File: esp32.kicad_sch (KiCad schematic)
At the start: 4 parts, among them U1 ESP32-S3-WROOM-1

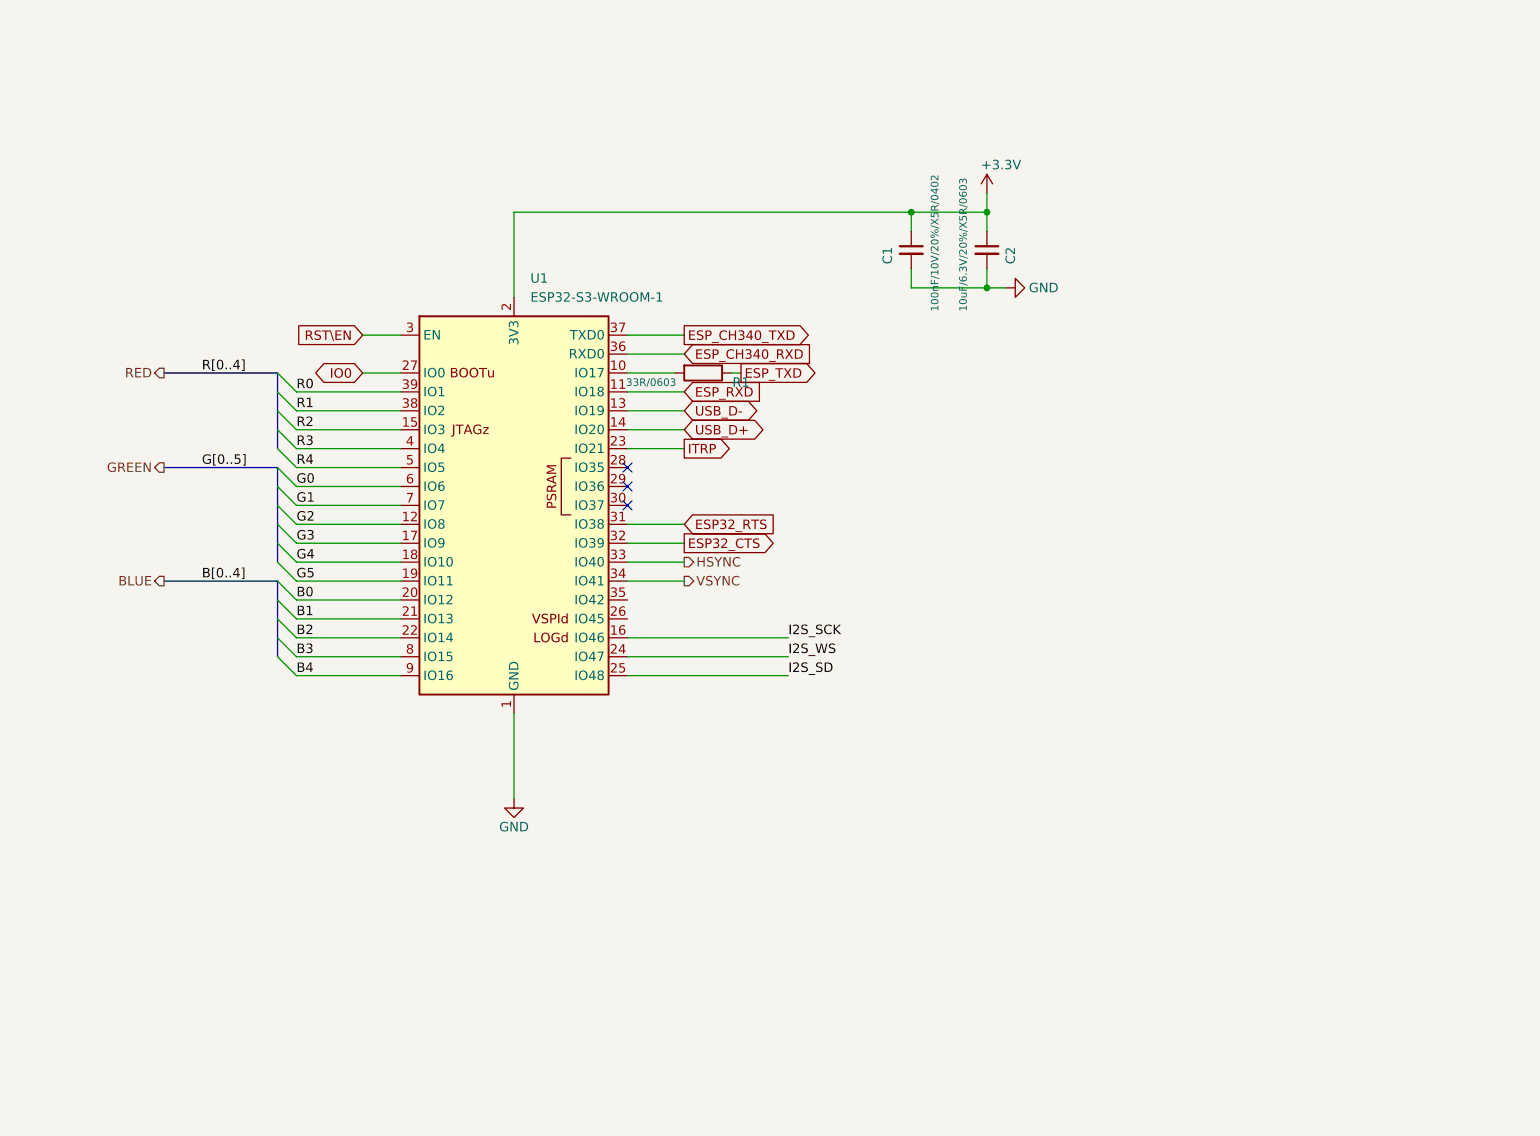
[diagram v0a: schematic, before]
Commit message: schematics finished, pcb routing 80%
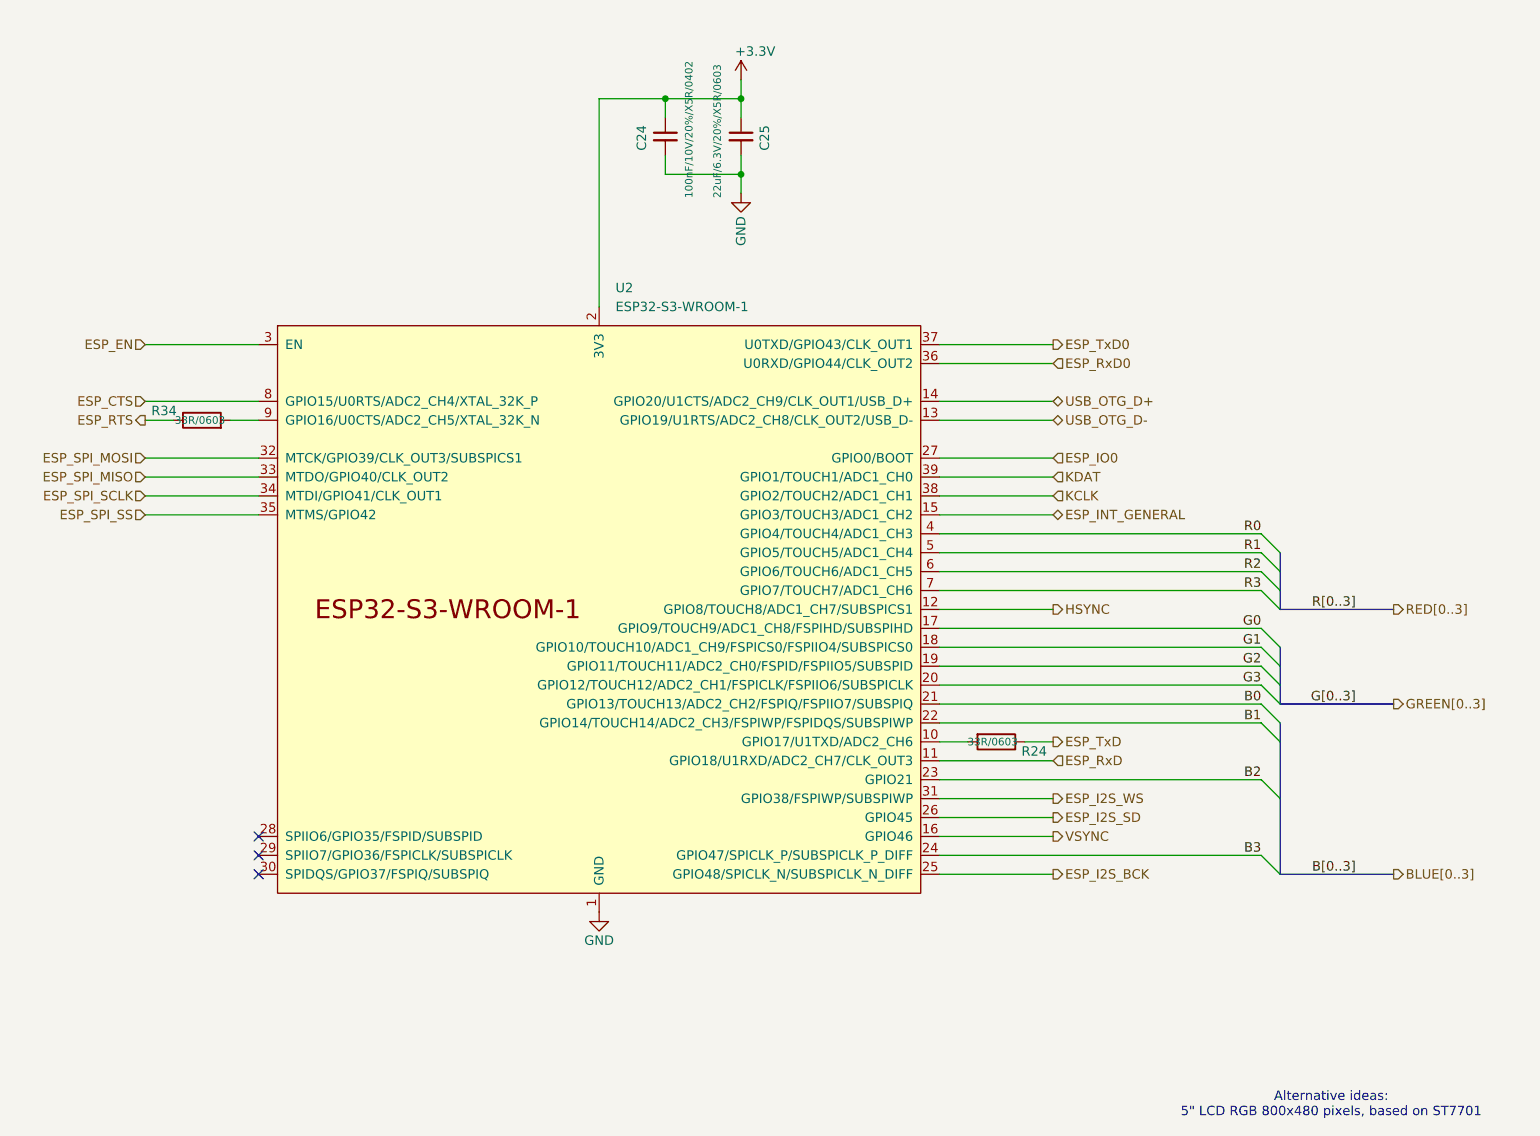
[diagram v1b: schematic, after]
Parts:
- removed C1: 100nF/10V/20%/X5R/0402, OLIMEX_RLC-FP:C_0402_5MIL_DWS, symbol AgonLight2_Rev_B:C
- removed C2: 10uF/6.3V/20%/X5R/0603, OLIMEX_RLC-FP:C_0603_5MIL_DWS, symbol AgonLight2_Rev_B:C
- removed R1: 33R/0603, OLIMEX_RLC-FP:R_0603_5MIL_DWS, symbol AgonLight2_Rev_B:R
- removed U1: ESP32-S3-WROOM-1, RF_Module:ESP32-S3-WROOM-1, symbol RF_Module:ESP32-S3-WROOM-1
- added C24: 100nF/10V/20%/X5R/0402, HexAgonFootprintsLibrary:C_0402_5MIL_DWS, symbol AgonLight2_Rev_B:C
- added C25: 22uF/6.3V/20%/X5R/0603, HexAgonFootprintsLibrary:C_0603_5MIL_DWS, symbol AgonLight2_Rev_B:C
- added R24, R34: 33R/0603, HexAgonFootprintsLibrary:R_0603_5MIL_DWS, symbol AgonLight2_Rev_B:R
- added U2: ESP32-S3-WROOM-1, Espressif:ESP32-S3-WROOM-1, symbol espressif:ESP32-S3-WROOM-1
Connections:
- net +3.3V: now also C24.1, C25.1, U2.2 (3V3)
- net B0: now also U2.21 (GPIO13/TOUCH13/ADC2_CH2/FSPIQ/FSPIIO7/SUBSPIQ)
- net B1: now also U2.22 (GPIO14/TOUCH14/ADC2_CH3/FSPIWP/FSPIDQS/SUBSPIWP)
- net B2: now also U2.23 (GPIO21)
- net B3: now also U2.24 (GPIO47/SPICLK_P/SUBSPICLK_P_DIFF)
- net G0: now also U2.17 (GPIO9/TOUCH9/ADC1_CH8/FSPIHD/SUBSPIHD)
- net G1: now also U2.18 (GPIO10/TOUCH10/ADC1_CH9/FSPICS0/FSPIIO4/SUBSPICS0)
- net G2: now also U2.19 (GPIO11/TOUCH11/ADC2_CH0/FSPID/FSPIIO5/SUBSPID)
- net G3: now also U2.20 (GPIO12/TOUCH12/ADC2_CH1/FSPICLK/FSPIIO6/SUBSPICLK)
- net GND: now also C24.2, C25.2, U2.1 (GND), U2.40 (GND), U2.41 (GND)
- net HSYNC: now also U2.12 (GPIO8/TOUCH8/ADC1_CH7/SUBSPICS1)
- net R0: now also U2.4 (GPIO4/TOUCH4/ADC1_CH3)
- net R1: now also U2.5 (GPIO5/TOUCH5/ADC1_CH4)
- net R2: now also U2.6 (GPIO6/TOUCH6/ADC1_CH5)
- net R3: now also U2.7 (GPIO7/TOUCH7/ADC1_CH6)
- net VSYNC: now also U2.16 (GPIO46)
- new net: R34.2, U2.9 (GPIO16/U0CTS/ADC2_CH5/XTAL_32K_N)
- new net: R24.2, U2.10 (GPIO17/U1TXD/ADC2_CH6)
- new net ESP_CTS: U2.8 (GPIO15/U0RTS/ADC2_CH4/XTAL_32K_P)
- new net ESP_EN: U2.3 (EN)
- new net ESP_I2S_BCK: U2.25 (GPIO48/SPICLK_N/SUBSPICLK_N_DIFF)
- new net ESP_I2S_SD: U2.26 (GPIO45)
- new net ESP_I2S_WS: U2.31 (GPIO38/FSPIWP/SUBSPIWP)
- new net ESP_INT_GENERAL: U2.15 (GPIO3/TOUCH3/ADC1_CH2)
- new net ESP_IO0: U2.27 (GPIO0/BOOT)
- new net ESP_RTS: R34.1
- new net ESP_RxD: U2.11 (GPIO18/U1RXD/ADC2_CH7/CLK_OUT3)
- new net ESP_RxD0: U2.36 (U0RXD/GPIO44/CLK_OUT2)
- new net ESP_SPI_MISO: U2.33 (MTDO/GPIO40/CLK_OUT2)
- new net ESP_SPI_MOSI: U2.32 (MTCK/GPIO39/CLK_OUT3/SUBSPICS1)
- new net ESP_SPI_SCLK: U2.34 (MTDI/GPIO41/CLK_OUT1)
- new net ESP_SPI_SS: U2.35 (MTMS/GPIO42)
- new net ESP_TxD: R24.1
- new net ESP_TxD0: U2.37 (U0TXD/GPIO43/CLK_OUT1)
- new net KCLK: U2.38 (GPIO2/TOUCH2/ADC1_CH1)
- new net KDAT: U2.39 (GPIO1/TOUCH1/ADC1_CH0)
- new net USB_OTG_D+: U2.14 (GPIO20/U1CTS/ADC2_CH9/CLK_OUT1/USB_D+)
- new net USB_OTG_D-: U2.13 (GPIO19/U1RTS/ADC2_CH8/CLK_OUT2/USB_D-)
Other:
- note added: "Alternative ideas: 5" LCD RGB 800x480 pixels, based on ST7701"

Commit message: 1st production and BOM
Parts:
- C24: MfgNumber (none) -> GRM022R61A104KE01L
- C25: value 22uF/6.3V/20%/X5R/0603 -> 22uF/6.3V/20%/X5R/C0603; MfgNumber (none) -> GRM188R60J226MEA0D
- R24, R34: MfgNumber (none) -> ESR03EZPJ330
- U2: MfgNumber (none) -> ESP32-S3-WROOM-1-N16R8
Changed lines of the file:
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@@
 			)
 		)
-		(property "Value" "22uF/6.3V/20%/X5R/0603"
+		(property "Value" "22uF/6.3V/20%/X5R/C0603"
 			(at 150.495 52.705 90)
 			(effects
@@
 				)
 				(hide yes)
+			)
+		)
+		(property "Note" ""
+			(at 153.67 44.45 0)
+			(effects
+				(font
+					(size 1.27 1.27)
+				)
+			)
+		)
+		(property "MfgNumber" "GRM188R60J226MEA0D"
+			(at 153.67 44.45 0)
+			(effects
+				(font
+					(size 1.27 1.27)
+				)
 			)
 		)
@@
 			)
 		)
+		(property "Note" ""
+			(at 143.51 44.45 0)
+			(effects
+				(font
+					(size 1.27 1.27)
+				)
+			)
+		)
+		(property "MfgNumber" "GRM022R61A104KE01L"
+			(at 143.51 44.45 0)
+			(effects
+				(font
+					(size 1.27 1.27)
+				)
+			)
+		)
 		(pin "1"
 		)
@@
 				)
 				(hide yes)
+			)
+		)
+		(property "Note" ""
+			(at 81.28 82.55 0)
+			(effects
+				(font
+					(size 1.27 1.27)
+				)
+			)
+		)
+		(property "MfgNumber" "ESR03EZPJ330"
+			(at 81.28 82.55 0)
+			(effects
+				(font
+					(size 1.27 1.27)
+				)
 			)
 		)
@@
 			)
 		)
+		(property "Note" ""
+			(at 134.62 107.95 0)
+			(effects
+				(font
+					(size 1.27 1.27)
+				)
+			)
+		)
+		(property "MfgNumber" "ESP32-S3-WROOM-1-N16R8"
+			(at 134.62 107.95 0)
+			(effects
+				(font
+					(size 1.27 1.27)
+				)
+			)
+		)
 		(pin "27"
 		)
@@
 			)
 		)
+		(property "Note" ""
+			(at 187.96 125.73 0)
+			(effects
+				(font
+					(size 1.27 1.27)
+				)
+			)
+		)
+		(property "MfgNumber" "ESR03EZPJ330"
+			(at 187.96 125.73 0)
+			(effects
+				(font
+					(size 1.27 1.27)
+				)
+			)
+		)
